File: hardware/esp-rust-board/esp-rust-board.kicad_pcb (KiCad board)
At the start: 2 copper layers, 22.9 x 63.5 mm, 55 parts, among them J1 USB4105-GF-A, Q1 DMG3415U, SW1 SW_Push, SW2 SW_Push, U1 SHTC3, U2 ICM-42670-P, U3 ESP32-C3-MINI-1, U4 Rust_Board, U5 SY8088, U6 MCP73831T-2ACI/OT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

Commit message: Add new components
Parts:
- added BZ1: Buzzer, Rust_Board:MLT-5020, F.Cu at (173.7, 90.9)
- added C17: 1uF 16V, Capacitor_SMD:C_0402_1005Metric, F.Cu at (168.7, 81.2)
- added C18: 1uF 16V, Capacitor_SMD:C_0402_1005Metric, F.Cu at (168.7, 83.2)
- added C19: 1uF, Capacitor_SMD:C_0402_1005Metric, F.Cu at (120.2, 113.8)
- added C20: 1uF, Capacitor_SMD:C_0402_1005Metric, F.Cu at (120.2, 115.8)
- added D10: SS24, Diode_SMD:D_SMA, F.Cu at (118.0, 98.1)
- added D11: SS24, Diode_SMD:D_SMA, F.Cu at (118.0, 102.6)
- added J2: MOTOR L, Connector_JST:JST_PH_B2B-PH-SM4-TB_1x02-1MP_P2.00mm_Vertical, F.Cu at (108.7, 101.1)
- added J3: MOTOR R, Connector_JST:JST_PH_B2B-PH-SM4-TB_1x02-1MP_P2.00mm_Vertical, F.Cu at (108.7, 110.6)
- added J4: SERVO L, Connector_JST:JST_PH_B3B-PH-SM4-TB_1x03-1MP_P2.00mm_Vertical, F.Cu at (105.5, 82.0)
- added J5: SERVO R, Connector_JST:JST_PH_B3B-PH-SM4-TB_1x03-1MP_P2.00mm_Vertical, F.Cu at (93.5, 82.0)
- added J6: LED L, Connector_JST:JST_PH_B2B-PH-SM4-TB_1x02-1MP_P2.00mm_Vertical, F.Cu at (173.4, 143.7)
- added J7: LED R, Connector_JST:JST_PH_B2B-PH-SM4-TB_1x02-1MP_P2.00mm_Vertical, F.Cu at (189.4, 143.7)
- added Q2: Si2319CDS, Package_TO_SOT_SMD:SOT-23, F.Cu at (116.3, 107.3)
- added Q3: Si2319CDS, Package_TO_SOT_SMD:SOT-23, F.Cu at (116.3, 111.9)
- added Q4: MMBT3904, Package_TO_SOT_SMD:SOT-23, F.Cu at (172.6, 96.4)
- added Q5: MMBT3904, Package_TO_SOT_SMD:SOT-23, F.Cu at (170.6, 150.4)
- added Q6: MMBT3904, Package_TO_SOT_SMD:SOT-23, F.Cu at (186.6, 150.4)
- added R13: 10kR 1%, Resistor_SMD:R_0402_1005Metric, F.Cu at (120.2, 105.9)
- added R16: 470R 1%, Resistor_SMD:R_0402_1005Metric, F.Cu at (120.2, 107.9)
- added R20: 470R 1%, Resistor_SMD:R_0402_1005Metric, F.Cu at (120.2, 109.9)
- added R21: 10kR 1%, Resistor_SMD:R_0402_1005Metric, F.Cu at (120.2, 111.8)
- added R22: 10kR 1%, Resistor_SMD:R_0402_1005Metric, F.Cu at (176.5, 95.0)
- added R23: 470R 1%, Resistor_SMD:R_0402_1005Metric, F.Cu at (176.5, 97.0)
- added R24: 470R 1%, Resistor_SMD:R_0402_1005Metric, F.Cu at (174.5, 149.0)
- added R25: 10kR 1%, Resistor_SMD:R_0402_1005Metric, F.Cu at (174.5, 151.0)
- added R26: 470R 1%, Resistor_SMD:R_0402_1005Metric, F.Cu at (190.5, 149.0)
- added R27: 10kR 1%, Resistor_SMD:R_0402_1005Metric, F.Cu at (190.5, 151.0)
- added TP1: TX, TestPoint:TestPoint_Pad_D1.0mm, F.Cu at (180.1, 140.0)
- added TP3: RX, TestPoint:TestPoint_Pad_D1.0mm, F.Cu at (180.1, 143.0)
- added U7: MAX17048G_T10, Package_DFN_QFN:TDFN-8-1EP_2x2mm_P0.5mm_EP0.8x1.2mm, F.Cu at (172.5, 82.2)
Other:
- board text removed: "0x68"
- board text removed: "0x70"

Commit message: Work in progress
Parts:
- removed C12, C13: DNP, Capacitor_SMD:C_0402_1005Metric
- removed C19, C20: 1uF, Capacitor_SMD:C_0402_1005Metric
- removed D10, D11: SS24, Diode_SMD:D_SMA
- removed J4: SERVO L, Connector_JST:JST_PH_B3B-PH-SM4-TB_1x03-1MP_P2.00mm_Vertical
- removed J5: SERVO R, Connector_JST:JST_PH_B3B-PH-SM4-TB_1x03-1MP_P2.00mm_Vertical
- removed J6: LED L, Connector_JST:JST_PH_B2B-PH-SM4-TB_1x02-1MP_P2.00mm_Vertical
- removed J7: LED R, Connector_JST:JST_PH_B2B-PH-SM4-TB_1x02-1MP_P2.00mm_Vertical
- removed Q2, Q3: Si2319CDS, Package_TO_SOT_SMD:SOT-23
- removed Q5, Q6: MMBT3904, Package_TO_SOT_SMD:SOT-23
- removed R12: DNP, Resistor_SMD:R_0402_1005Metric
- removed R13, R21, R25, R27: 10kR 1%, Resistor_SMD:R_0402_1005Metric
- removed R16, R20, R24, R26: 470R 1%, Resistor_SMD:R_0402_1005Metric
- removed TP1: TX, TestPoint:TestPoint_Pad_D1.0mm
- removed TP3: RX, TestPoint:TestPoint_Pad_D1.0mm
- removed Y1: 32.768Hz, Crystal:Crystal_SMD_3215-2Pin_3.2x1.5mm
- added J8: BATTERY, Connector_JST:JST_EH_B2B-EH-A_1x02_P2.50mm_Vertical, F.Cu at (170.8, 86.8)
- D9: value WS2812B -> LED; footprint LED_SMD:LED_SK6812MINI_PLCC4_3.5x3.5mm_P1.75mm -> LED_SMD:LED_0603_1608Metric
- J2: value MOTOR L -> DF37C-30DP-0.4V_51_; footprint Connector_JST:JST_PH_B2B-PH-SM4-TB_1x02-1MP_P2.00mm_Vertical -> Rust_Board:HRS_DF37C-30DP-0.4V_51_; moved to B.Cu
- J3: value MOTOR R -> DF37C-30DP-0.4V_51_; footprint Connector_JST:JST_PH_B2B-PH-SM4-TB_1x02-1MP_P2.00mm_Vertical -> Rust_Board:HRS_DF37C-30DP-0.4V_51_; moved to B.Cu
- R11: value 0R 1% -> 470R 1%
- SW1: value SW_Push -> RESET
- SW2: value SW_Push -> BOOT
- moved J3 48.4 mm to (157.1, 112.5), turned to 90 degrees
- moved J2 32.5 mm to (139.1, 112.5), turned to 90 degrees
- moved D2 32.4 mm to (141.8, 111.7), turned to 90 degrees
- moved SW2 31.9 mm to (123.9, 108.9), turned to 0 degrees
- moved R10 29.3 mm to (143.5, 110.3), turned to -90 degrees
- moved BZ1 21.7 mm to (156.8, 104.5), turned to -90 degrees
- moved SW1 19.8 mm to (123.9, 104.2), turned to 0 degrees
- moved U7 17.0 mm to (156.0, 86.2), turned to 90 degrees
- moved C18 14.5 mm to (155.2, 88.5), turned to 180 degrees
- moved C17 12.9 mm to (158.0, 88.5)
- moved Q4 12.3 mm to (166.2, 107.0), turned to -90 degrees
- moved C14 9.32 mm to (152.1, 84.4), turned to 90 degrees
- moved R11 4.31 mm to (144.5, 95.0)
- moved D9 2.55 mm to (147.8, 95.0)
- moved D3 2.02 mm to (141.8, 115.0)
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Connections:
- D9 pad 1: +3V3 -> GND
- D9 pad 2: unconnected-(D9-DOUT-Pad2) -> Net-(D9-A)
- J2 pad 1: +BATT -> GND
- J2 pad 2: Net-(D10-A) -> unconnected-(J2-Pad2)
- J3 pad 1: +BATT -> +5V
- J3 pad 2: Net-(D11-A) -> +BATT
- R1 pad 2: ENABLE -> Net-(U5-EN)
- R10 pad 1: IO7 -> +3V3
- R11 pad 2: Net-(D9-DIN) -> Net-(D9-A)
- U5 pad 1: ENABLE -> Net-(U5-EN)
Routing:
- net VBUS: track 39.3 -> 13.3 mm, vias 7 -> 5
- net IO8_SCL: track 74.8 -> 49.6 mm, vias 4 -> 3
- net ENABLE: track 24.5 -> 0.00 mm, vias 2 -> 0
- net CHIP_PU: track 28.5 -> 5.33 mm
- net +5V: track 10.7 -> 24.5 mm
- net Net-(D9-DIN): track 10.5 -> 0.00 mm
- net IO10_SDA: track 54.8 -> 45.6 mm
- net +3V3: track 65.4 -> 72.0 mm
- net IO2: track 23.8 -> 29.1 mm
- net IO7: track 33.5 -> 29.3 mm, vias 2 -> 1
- net IO9_BOOT: track 51.5 -> 47.6 mm
- net IO1: track 16.8 -> 13.0 mm
- net USB_D+: track 59.9 -> 57.3 mm, vias 3 -> 2
- net Net-(U5-EN): track 0.00 -> 2.42 mm
- net IO0: track 11.6 -> 9.36 mm
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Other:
- board text added: "FLIGHT COMPUTER"
- board text removed: "10"
- board text removed: "19"
- board text removed: "3V3"
- board text removed: "5V"
- board text removed: "EN"
- board text removed: "GND"
- board text removed: "NC"
- board text removed: "RST"

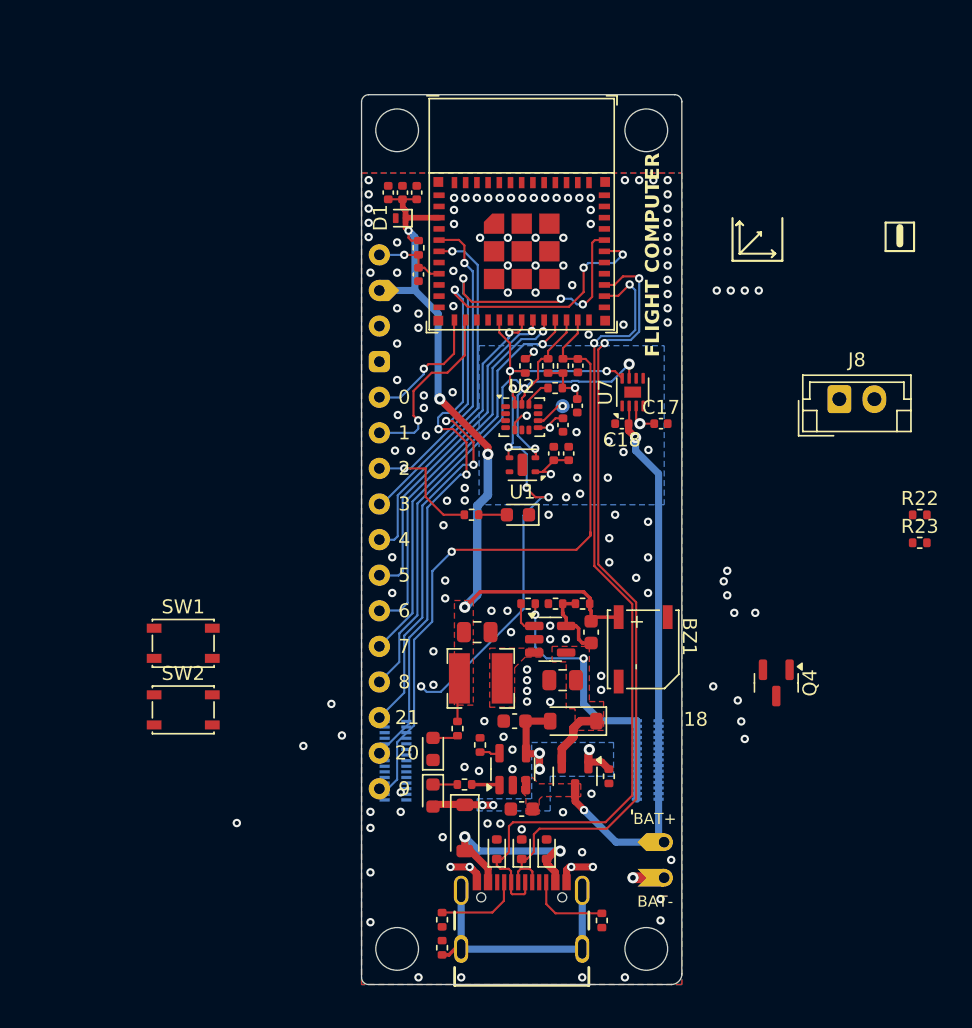
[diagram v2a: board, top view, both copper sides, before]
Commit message: Add magnamometer and barometer and rearrange items
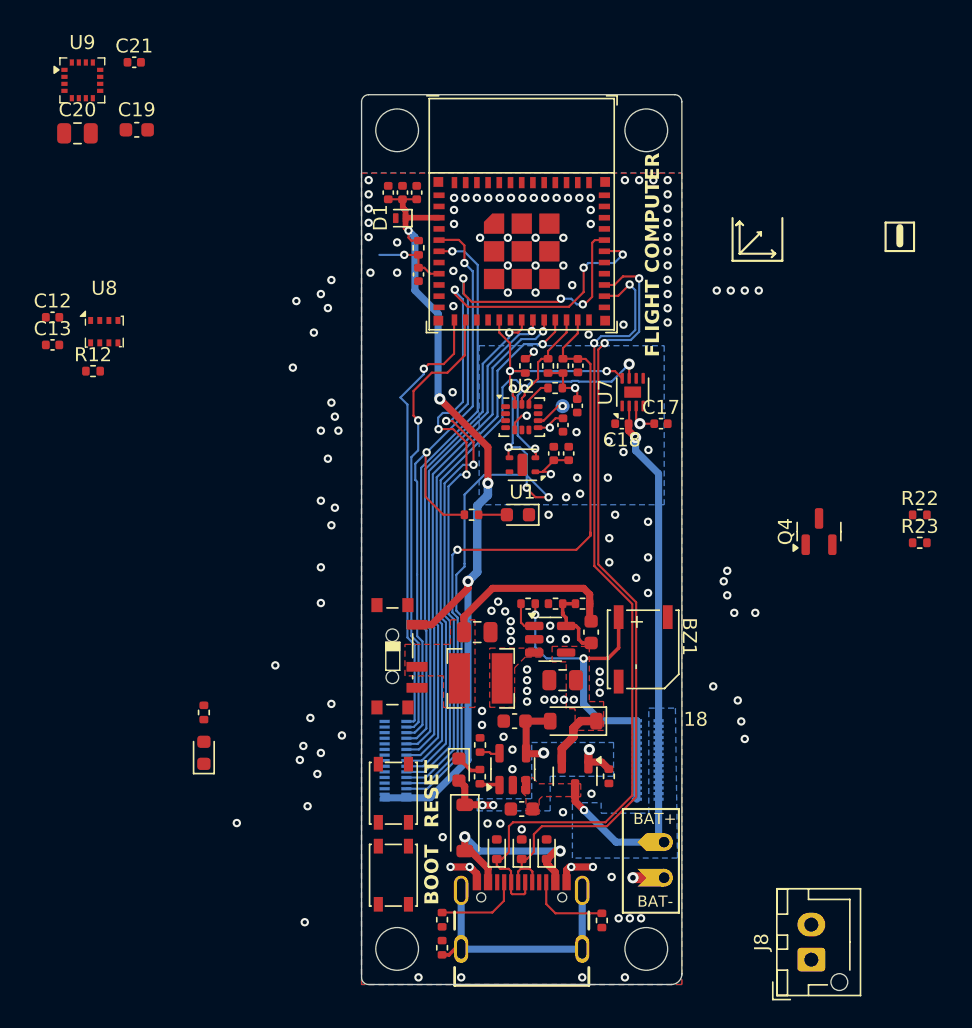
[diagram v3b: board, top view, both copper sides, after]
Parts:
- added C12: 10nF 10V, Capacitor_SMD:C_0402_1005Metric, F.Cu at (114.6, 80.9)
- added C13: 100nF 10V, Capacitor_SMD:C_0402_1005Metric, F.Cu at (114.6, 82.9)
- added C19: 4.7uF 16V, Capacitor_SMD:C_0603_1608Metric, F.Cu at (120.6, 67.5)
- added C20: 10uF 16V, Capacitor_SMD:C_0805_2012Metric, F.Cu at (116.4, 67.8)
- added C21: 0.22uF, Capacitor_SMD:C_0402_1005Metric, F.Cu at (120.4, 62.7)
- added R12: 10kR 1%, Resistor_SMD:R_0402_1005Metric, F.Cu at (117.5, 84.8)
- added SW3: SW_DPDT_x2, Rust_Board:SW_SPDT_PCM12, F.Cu at (139.2, 105.1)
- added U8: BMP280, Package_LGA:Bosch_LGA-8_2x2.5mm_P0.65mm_ClockwisePinNumbering, F.Cu at (118.3, 81.9)
- added U9: QMC5883L, Package_LGA:LGA-16_3x3mm_P0.5mm, F.Cu at (116.7, 64.0)
- J2: value DF37C-30DP-0.4V_51_ -> GPIO
- J3: value DF37C-30DP-0.4V_51_ -> POWER
- J8: footprint Connector_JST:JST_EH_B2B-EH-A_1x02_P2.50mm_Vertical -> Connector_JST:JST_XH_B2B-XH-AM_1x02_P2.50mm_Vertical
- moved J8 40.0 mm to (168.8, 126.8), turned to 90 degrees
- moved SW2 19.1 mm to (138.9, 120.7), turned to 90 degrees
- moved SW1 18.4 mm to (138.9, 114.9), turned to 90 degrees
- moved R10 18.1 mm to (125.4, 109.1)
- moved D2 16.4 mm to (125.4, 112.0)
- moved Q4 11.2 mm to (169.3, 96.2), turned to 90 degrees
- moved D3 2.62 mm to (143.6, 113.2)
- moved R14 1.23 mm to (145.1, 113.7), turned to 90 degrees
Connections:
- BZ1 pad 1: +3V3 -> +5V
- C6 pad 1: +3V3 -> /POWER
- C7 pad 1: +3V3 -> /POWER
- J2 pad 1: GND -> +3V3
- J2 pad 10: unconnected-(J2-Pad10) -> IO20_RX
- J2 pad 12: unconnected-(J2-Pad12) -> IO21_TX
- J2 pad 14: unconnected-(J2-Pad14) -> IO8_SCL
- J2 pad 16: unconnected-(J2-Pad16) -> IO7
- J2 pad 18: unconnected-(J2-Pad18) -> IO6
- J2 pad 2: unconnected-(J2-Pad2) -> +3V3
- J2 pad 20: unconnected-(J2-Pad20) -> IO5
- J2 pad 22: unconnected-(J2-Pad22) -> IO4
- J2 pad 24: unconnected-(J2-Pad24) -> IO3
- J2 pad 26: unconnected-(J2-Pad26) -> IO2
- J2 pad 28: unconnected-(J2-Pad28) -> IO1
- J2 pad 3: GND -> +3V3
- J2 pad 30: unconnected-(J2-Pad30) -> IO0
- J2 pad 4: unconnected-(J2-Pad4) -> +3V3
- J2 pad 5: GND -> unconnected-(J2-Pad5)
- J2 pad 6: unconnected-(J2-Pad6) -> IO10_SDA
- J2 pad 7: GND -> unconnected-(J2-Pad7)
- J2 pad 8: unconnected-(J2-Pad8) -> IO9_BOOT
- J2 pad 9: GND -> unconnected-(J2-Pad9)
- L1 pad 2: +3V3 -> /POWER
- R2 pad 1: +3V3 -> /POWER
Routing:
- net IO0: track 9.36 -> 31.9 mm
- net IO1: track 13.0 -> 32.5 mm
- net IO2: track 29.1 -> 46.3 mm
- net IO3: track 23.3 -> 39.8 mm
- net IO4: track 20.9 -> 34.8 mm
- net /POWER: track 0.00 -> 13.7 mm
- net IO10_SDA: track 45.6 -> 57.8 mm, vias 7 -> 6
- net IO5: track 23.9 -> 35.6 mm
- net IO6: track 27.0 -> 36.6 mm
- net IO7: track 29.3 -> 37.7 mm
- net IO8_SCL: track 49.6 -> 55.8 mm
- net +5V: track 24.5 -> 29.5 mm
- net IO21_TX: track 52.5 -> 56.6 mm
- net +3V3: track 72.0 -> 75.6 mm
- net IO20_RX: track 55.3 -> 57.4 mm
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- added copper zone on B.Cu, net +BATT
- added copper zone on F.Cu, net /POWER
- removed copper zone on F.Cu, net +3V3
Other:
- board text added: "BOOT"
- board text added: "RESET"
- board text removed: "0"
- board text removed: "2"
- board text removed: "20"
- board text removed: "21"
- board text removed: "3"
- board text removed: "4"
- board text removed: "5"
- board text removed: "6"
- board text removed: "7"
- board text removed: "8"
- board text removed: "9"

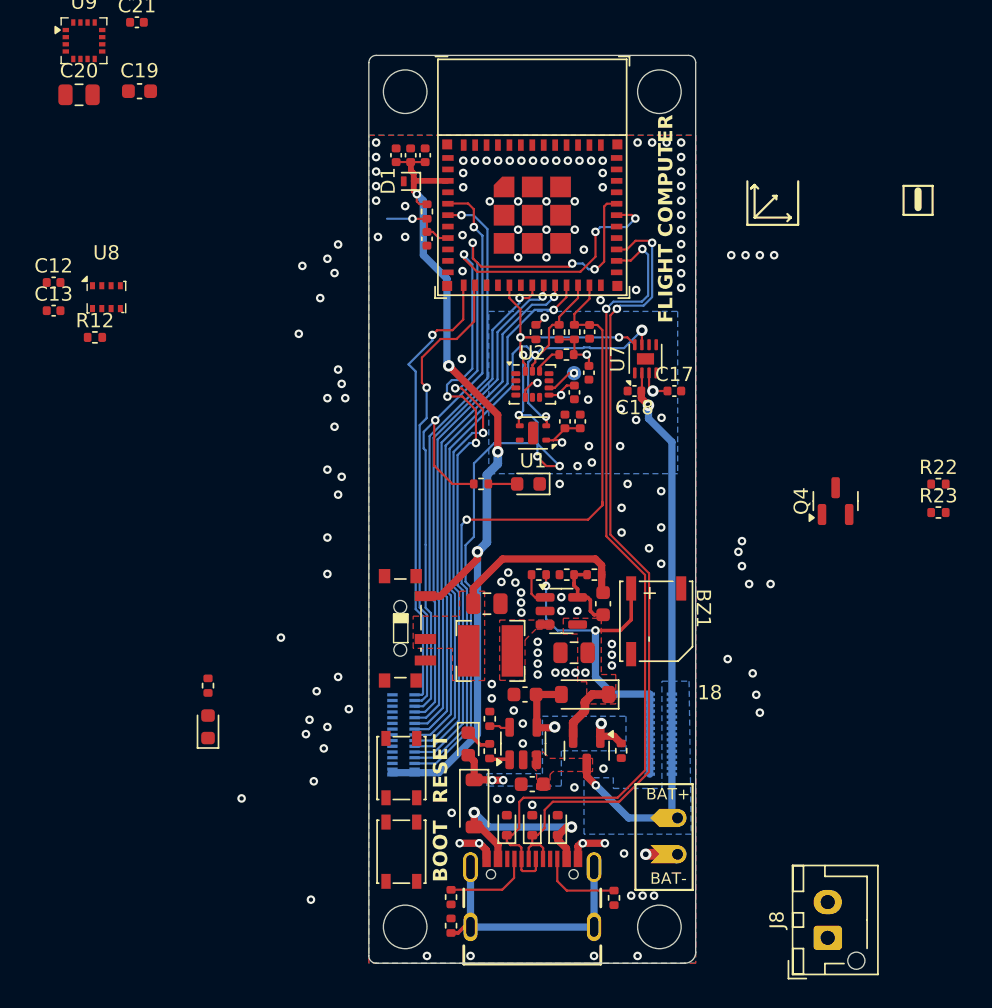
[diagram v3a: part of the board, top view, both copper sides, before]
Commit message: Reorganize PCB, remove piezo, temperature sensor and expansion connections
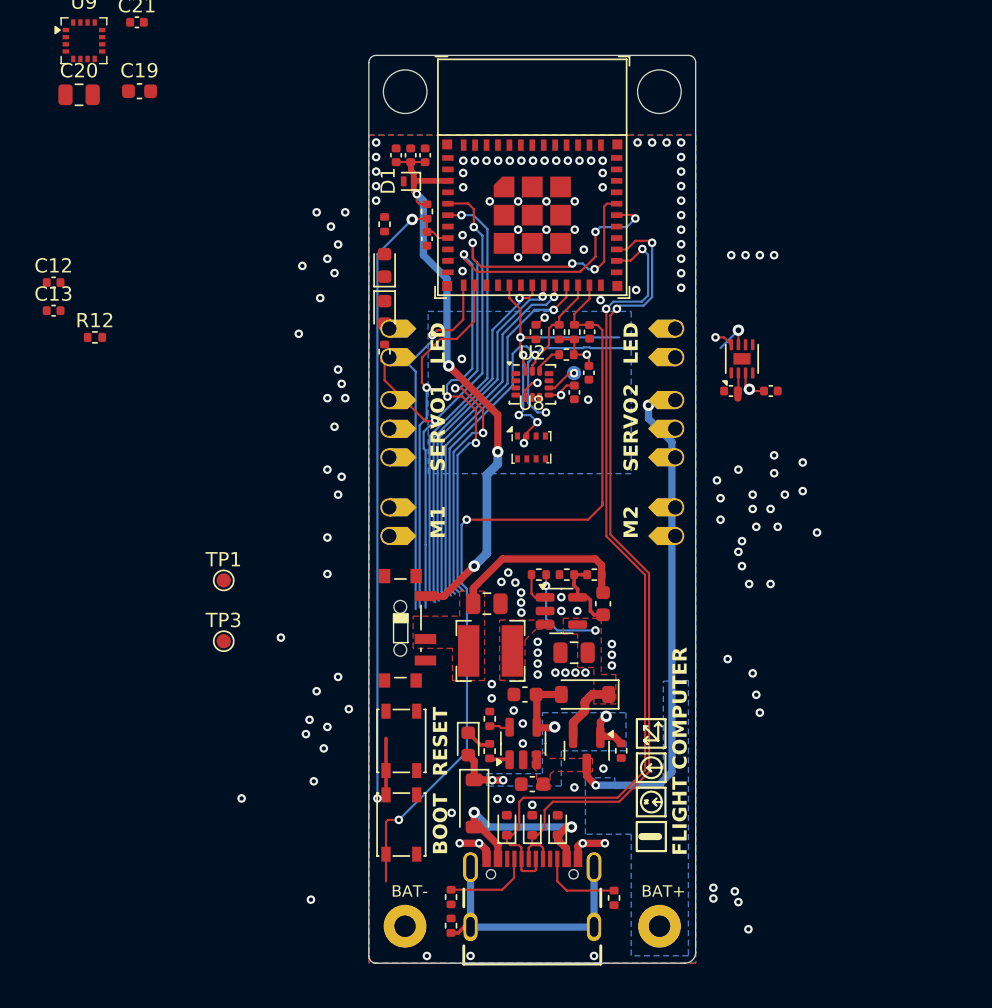
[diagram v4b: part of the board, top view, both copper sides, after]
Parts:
- removed BZ1: Buzzer, Rust_Board:MLT-5020
- removed C1: 10nF 10V, Capacitor_SMD:C_0402_1005Metric
- removed C3: 100nF 10V, Capacitor_SMD:C_0402_1005Metric
- removed J2: GPIO, Rust_Board:HRS_DF37C-30DP-0.4V_51_
- removed J3: POWER, Rust_Board:HRS_DF37C-30DP-0.4V_51_
- removed J8: BATTERY, Connector_JST:JST_XH_B2B-XH-AM_1x02_P2.50mm_Vertical
- removed Q4: MMBT3904, Package_TO_SOT_SMD:SOT-23
- removed R22: 10kR 1%, Resistor_SMD:R_0402_1005Metric
- removed R23: 470R 1%, Resistor_SMD:R_0402_1005Metric
- removed U1: SHTC3, Sensor_Humidity:Sensirion_DFN-4-1EP_2x2mm_P1mm_EP0.7x1.6mm
- added TP1: TestPoint, TestPoint:TestPoint_Pad_D1.0mm, F.Cu at (126.5, 101.8)
- added TP3: TestPoint, TestPoint:TestPoint_Pad_D1.0mm, F.Cu at (126.5, 106.0)
- moved R10 34.6 mm to (137.8, 76.8)
- moved D2 34.6 mm to (137.8, 79.7)
- moved U8 31.5 mm to (148.0, 92.5)
- moved D9 15.7 mm to (137.8, 83.0), turned to -90 degrees
- moved R11 11.5 mm to (137.8, 85.8), turned to 90 degrees
- moved C17 6.75 mm to (164.8, 88.5)
- moved C18 6.75 mm to (162.0, 88.5)
- moved U7 6.75 mm to (162.8, 86.2)
- moved SW1 1.90 mm to (138.9, 113.0)
- moved SW2 1.90 mm to (138.9, 118.8)
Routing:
- net CHIP_PU: track 5.33 -> 49.9 mm, vias 1 -> 2
- net IO10_SDA: track 57.8 -> 23.5 mm
- net +3V3: track 75.6 -> 52.4 mm, vias 10 -> 9
- net +5V: track 29.5 -> 11.4 mm
- net IO20_RX: track 57.4 -> 43.9 mm
- net IO8_SCL: track 55.8 -> 42.9 mm
- net IO21_TX: track 56.6 -> 43.8 mm
- net IO7: track 37.7 -> 26.2 mm
- net IO6: track 36.6 -> 25.9 mm
- net IO5: track 35.6 -> 25.6 mm
- net IO4: track 34.8 -> 25.5 mm
- net IO9_BOOT: track 47.1 -> 56.1 mm, vias 1 -> 2
- net IO3: track 39.8 -> 31.1 mm
- net IO2: track 46.3 -> 38.2 mm
- net IO1: track 32.5 -> 25.1 mm
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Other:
- outline, holes or cut-outs redrawn
- board text removed: "18"

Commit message: Add missing components
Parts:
- added C1: 1uF, Capacitor_SMD:C_0402_1005Metric, F.Cu at (110.9, 41.0)
- added C3: 1uF, Capacitor_SMD:C_0402_1005Metric, F.Cu at (85.7, 40.3)
- added D10: SS24, Diode_SMD:D_SOD-123, F.Cu at (101.9, 47.3)
- added D11: SS24, Diode_SMD:D_SOD-123, F.Cu at (76.7, 46.6)
- added J2: MOTOR L, Connector_JST:JST_PH_B2B-PH-SM4-TB_1x02-1MP_P2.00mm_Vertical, F.Cu at (104.3, 41.3)
- added J3: MOTOR R, Connector_JST:JST_PH_B2B-PH-SM4-TB_1x02-1MP_P2.00mm_Vertical, F.Cu at (79.1, 40.6)
- added J5: LED L, Connector_JST:JST_PH_B2B-PH-SM4-TB_1x02-1MP_P2.00mm_Vertical, F.Cu at (125.8, 41.7)
- added J6: LED R, Connector_JST:JST_PH_B2B-PH-SM4-TB_1x02-1MP_P2.00mm_Vertical, F.Cu at (139.3, 41.8)
- added Q2: Si2319CDS, Package_TO_SOT_SMD:SOT-23, F.Cu at (107.3, 48.0)
- added Q3: Si2319CDS, Package_TO_SOT_SMD:SOT-23, F.Cu at (82.1, 47.3)
- added Q4: MMBT3904, Package_TO_SOT_SMD:SOT-23, F.Cu at (123.0, 48.4)
- added Q5: MMBT3904, Package_TO_SOT_SMD:SOT-23, F.Cu at (136.5, 48.5)
- added R13: 470R 1%, Resistor_SMD:R_0402_1005Metric, F.Cu at (110.9, 37.0)
- added R16: 10kR 1%, Resistor_SMD:R_0402_1005Metric, F.Cu at (110.9, 39.0)
- added R20: 470R 1%, Resistor_SMD:R_0402_1005Metric, F.Cu at (85.7, 36.3)
- added R21: 10kR 1%, Resistor_SMD:R_0402_1005Metric, F.Cu at (85.7, 38.3)
- added R22: 470R 1%, Resistor_SMD:R_0402_1005Metric, F.Cu at (126.9, 47.0)
- added R23: 10kR 1%, Resistor_SMD:R_0402_1005Metric, F.Cu at (126.9, 49.0)
- added R24: 470R 1%, Resistor_SMD:R_0402_1005Metric, F.Cu at (140.4, 47.1)
- added R25: 10kR 1%, Resistor_SMD:R_0402_1005Metric, F.Cu at (140.4, 49.1)
